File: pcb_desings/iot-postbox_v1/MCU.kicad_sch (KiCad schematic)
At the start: 28 parts, among them U1 ESP32-S2, U2 W25Q128JVS, U3 LY68L6400SLIT, Y1 40MHz

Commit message: Added iot-postbox_v1 sch to v1.1. Added minor documentation
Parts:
- R3: Populated (none) -> TBD
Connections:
- net GPIO18: now reaches R3.1, U1.24 (GPIO18/ADC2_CH7/DAC_2)
- net 3V3_LDO2_EN renamed LDO2_EN
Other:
- note added: "Add a 499 series resistor to GPIO43 to supress U0TXD 80MHz harmonics. Only if used as UART?"
- note added: "GPIO18 - Pull up to avoid U1RXD booting issues? Not required if this pin is not used?"
- note removed: "GPIO18 - Pull up to avoid U1RXD booting issues?"
- moved on the sheet: AE1, AE4, C10, C12, C13, C14, C15, C2, C3, C5, C6, C7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

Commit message: Added some sch info
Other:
- note added: "Add a 499Ohm series resistor to GPIO43 to supress U0TXD 80MHz harmonics. Only if used as UART?"
- note removed: "Add a 499 series resistor to GPIO43 to supress U0TXD 80MHz harmonics. Only if used as UART?"
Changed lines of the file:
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@@
     (effects (font (size 2.54 2.54)) (justify left bottom))
   )
-  (text "Add a 499 series resistor to GPIO43\nto supress U0TXD 80MHz harmonics.\nOnly if used as UART?"
+  (text "Add a 499Ohm series resistor to GPIO43\nto supress U0TXD 80MHz harmonics.\nOnly if used as UART?"
     (at 199.39 48.26 0)
     (effects (font (size 1 1)) (justify left bottom))

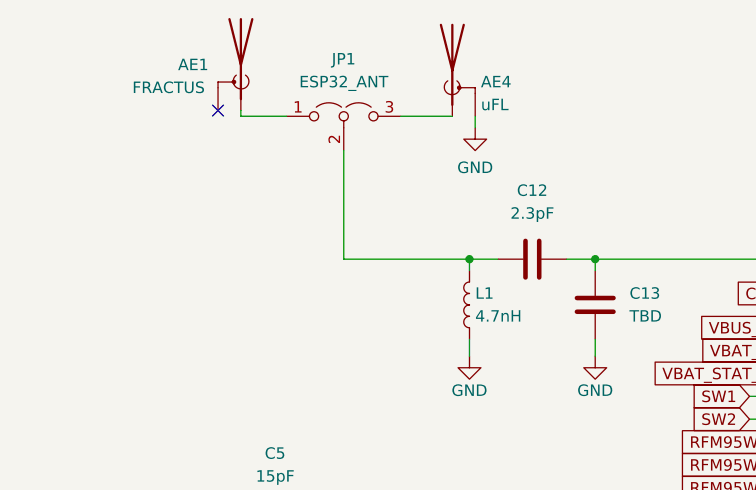
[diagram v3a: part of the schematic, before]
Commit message: Created iot-postbox v1.2 migrating to kicad v9. Fixed missing 3d designs, replaced horizontal footprints for some connectors.
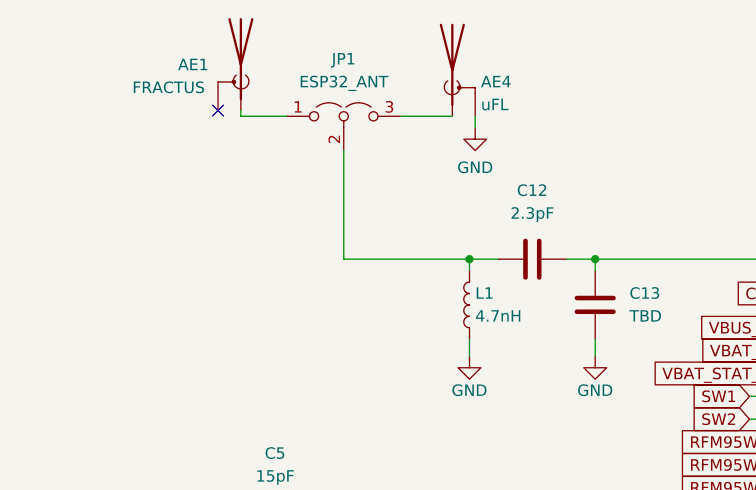
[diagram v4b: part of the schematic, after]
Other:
- company: (none) -> @paclema
